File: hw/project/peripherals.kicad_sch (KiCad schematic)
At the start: 71 parts, among them J1 Battery, J10 2.54 Comm, J11 Voltage Monitor, J12 SPI, J13 I2C, J14 CONN HEADER VERT 10POS 2MM, J2 Hall, J3 FTSH-107-01-L-DV-K-A, J4 Serial, J5 Phases, J8 Throttle, J9 CAN, SW3 USER, U2 ATA6561-GAQW-N

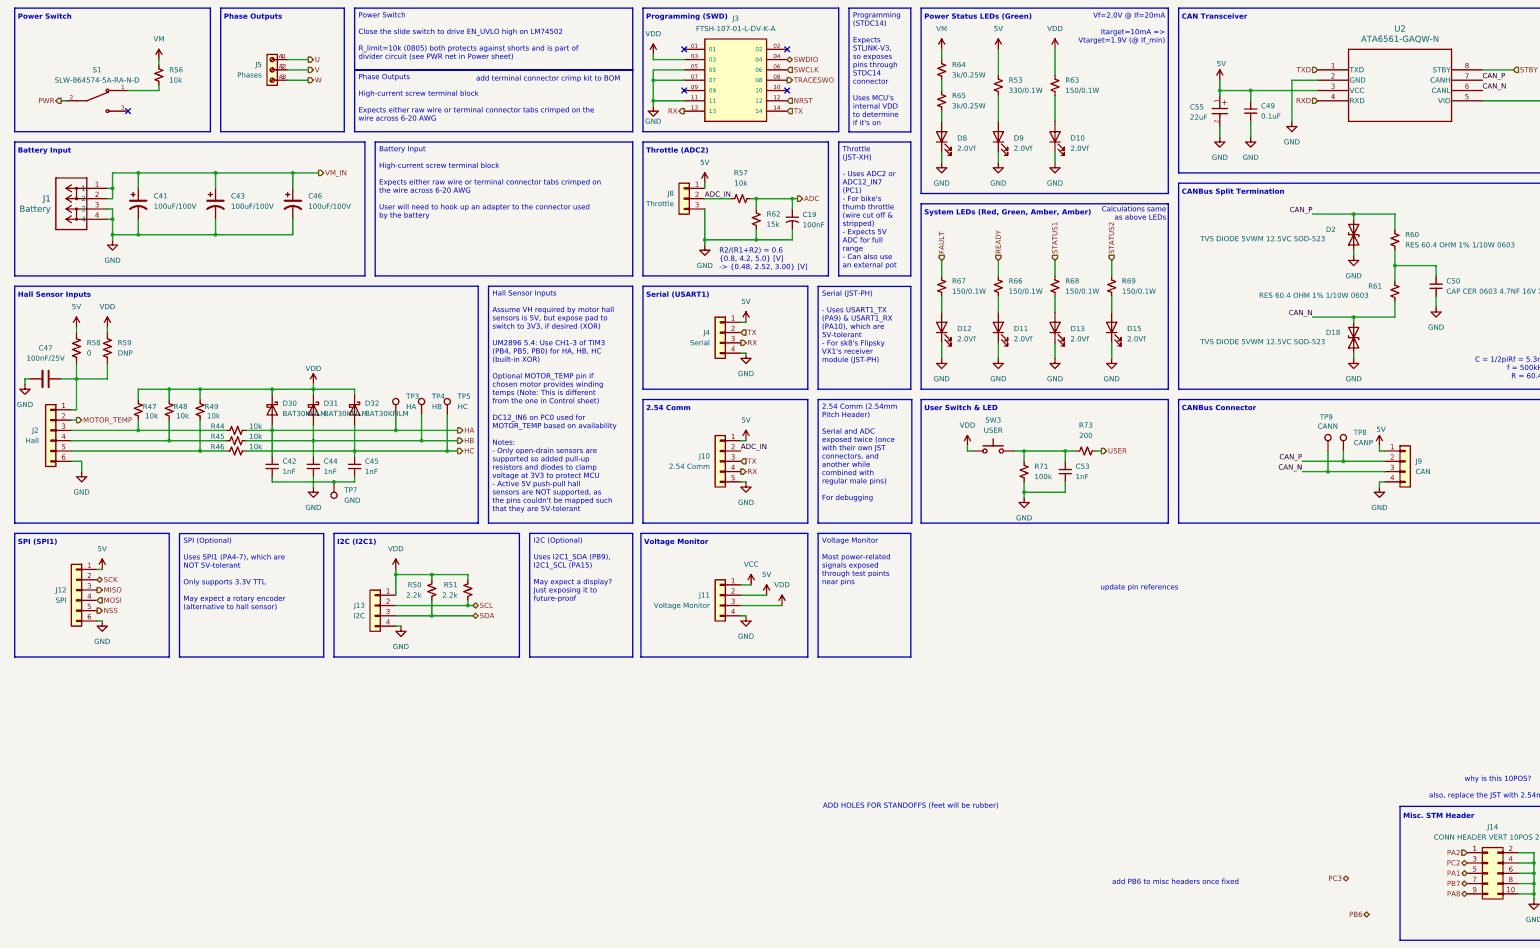
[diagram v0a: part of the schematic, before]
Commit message: Prettify root sheet
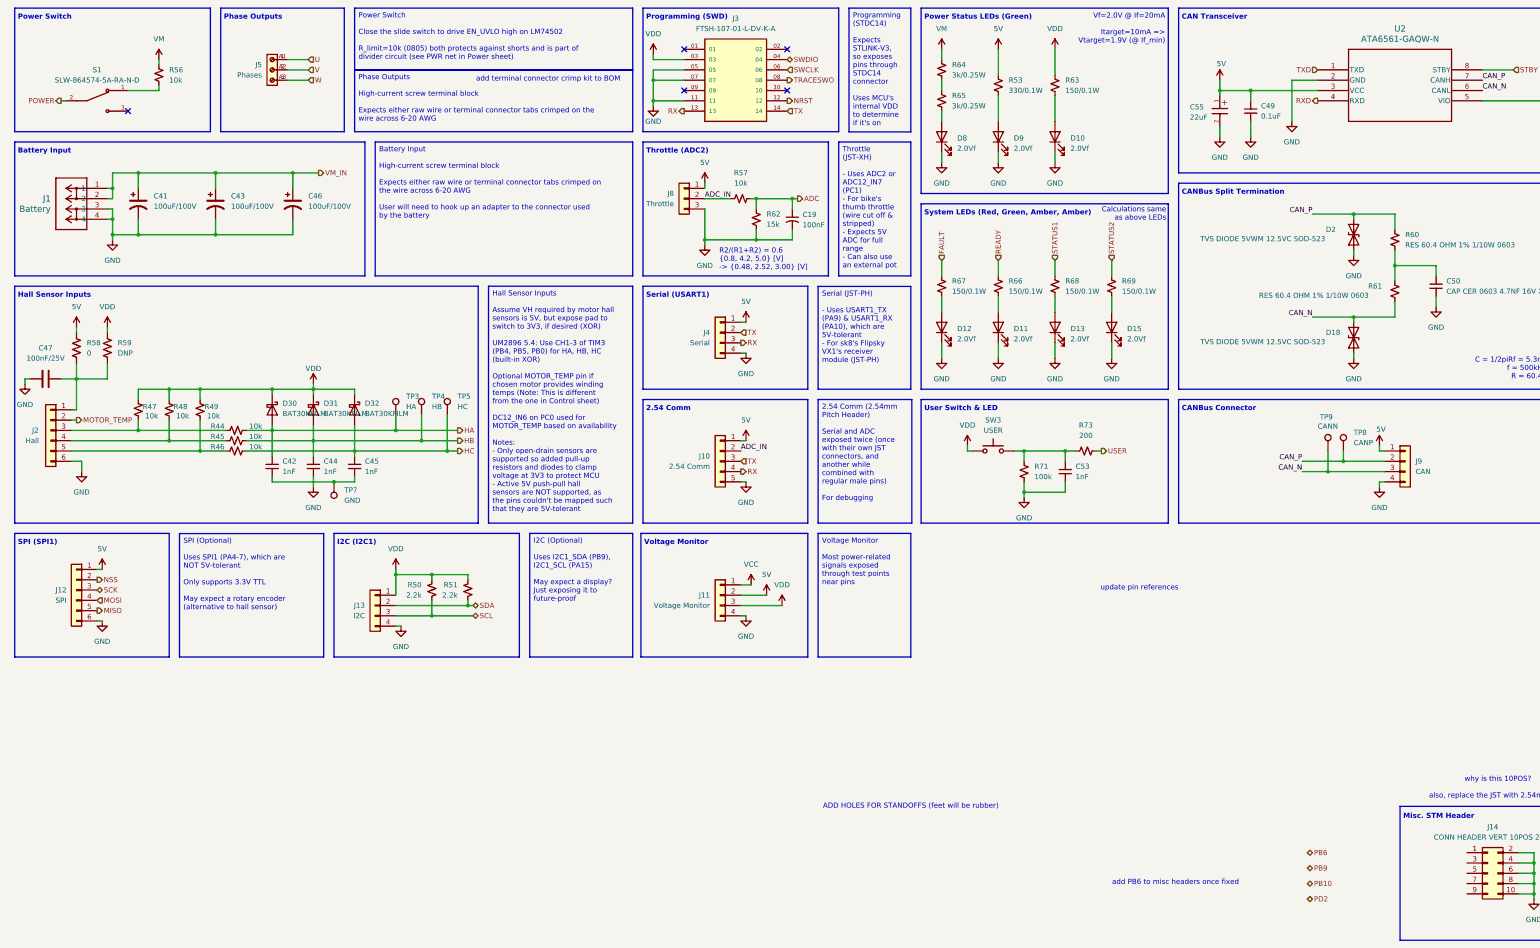
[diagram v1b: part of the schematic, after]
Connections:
- net MISO: now also J12.5 (Pin_5); no longer J12.3 (Pin_3)
- net NSS: now also J12.2 (Pin_2); no longer J12.5 (Pin_5)
- net SCK: now also J12.3 (Pin_3); no longer J12.2 (Pin_2)
- net SCL: now also J13.3 (Pin_3), R50.2; no longer J13.2 (Pin_2), R51.2
- net SDA: now also J13.2 (Pin_2), R51.2; no longer J13.3 (Pin_3), R50.2
- net PA1: no longer names the net of J14.5 (Pin_5)
- net PA2: no longer names the net of J14.1 (Pin_1)
- net PA8: no longer names the net of J14.9 (Pin_9)
- net PB7: no longer names the net of J14.7 (Pin_7)
- net PC2: no longer names the net of J14.3 (Pin_3)
- net PWR renamed POWER

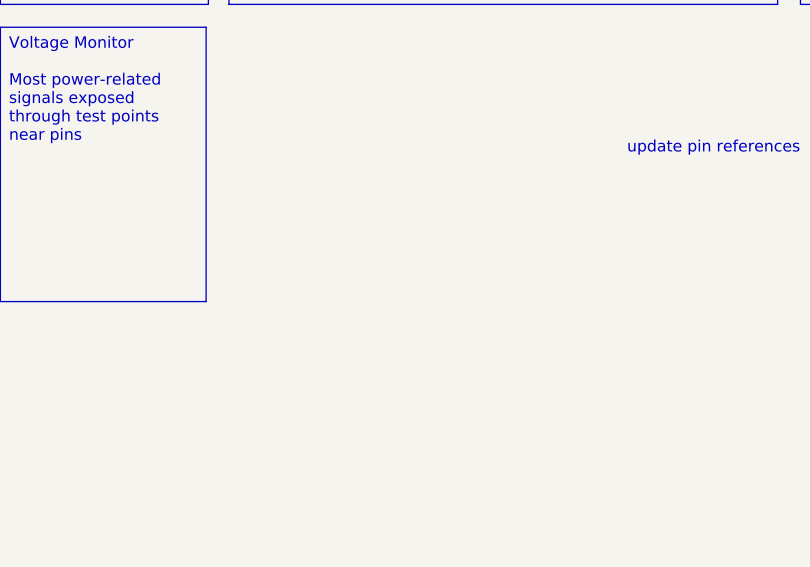
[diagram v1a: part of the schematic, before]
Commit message: Finished control sheet sensing. Need to work on OSC tomorrow
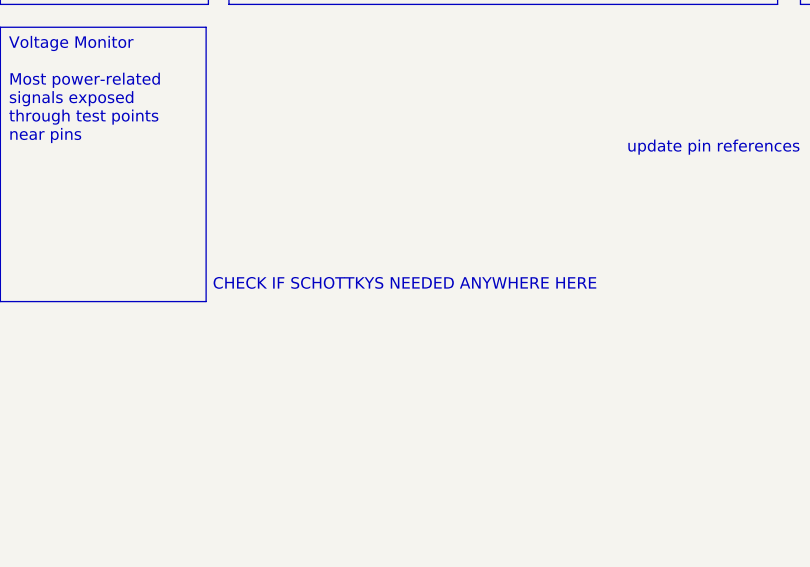
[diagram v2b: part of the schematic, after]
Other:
- note added: "CHECK IF SCHOTTKYS NEEDED ANYWHERE HERE"
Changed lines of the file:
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@@
+		)
+	)
+	(text "CHECK IF SCHOTTKYS NEEDED ANYWHERE HERE"
+		(exclude_from_sim no)
+		(at 258.318 176.022 0)
+		(effects
+			(font
+				(size 1.27 1.27)
+				(color 255 4 4 1)
+			)
 		)
 	)

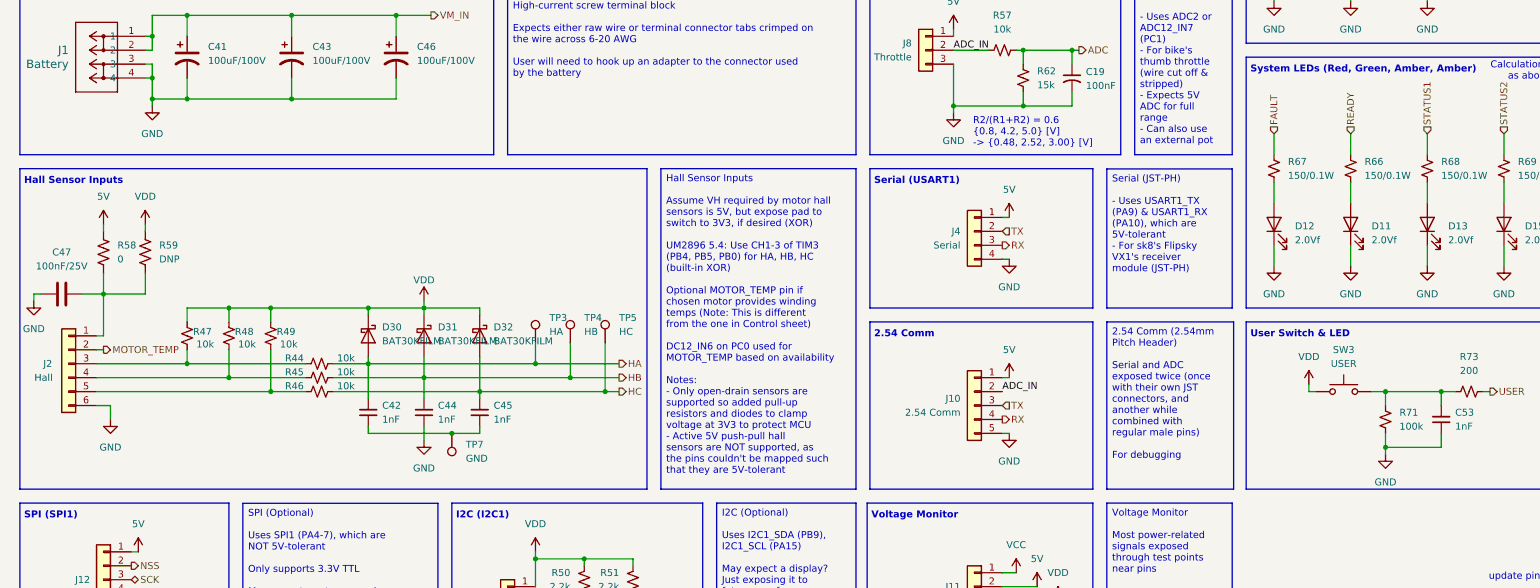
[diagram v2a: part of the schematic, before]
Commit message: Finalize phase voltage sensing
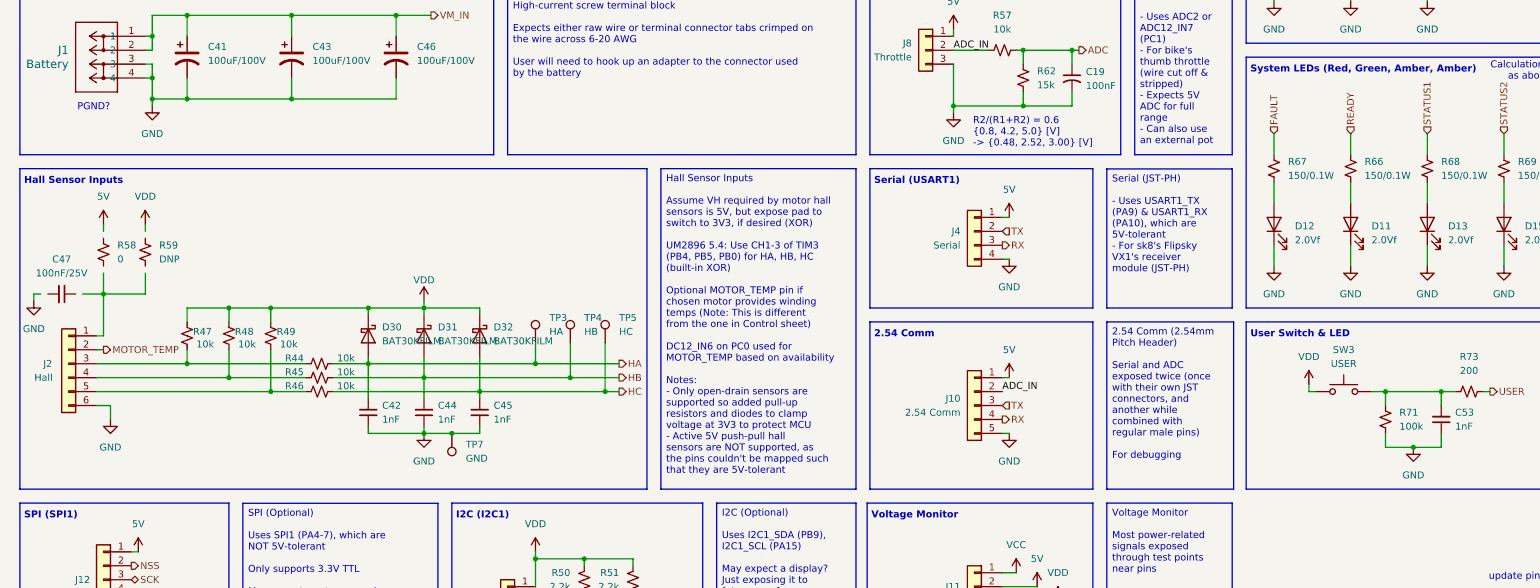
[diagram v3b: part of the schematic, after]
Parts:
- C47: symbol Device:C -> Device:C_Small
- R58, R59: symbol Device:R_US -> Device:R_Small_US
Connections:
- net 5V: no longer R58.1
- net GND: now also C42.1, C45.1, TP7.1; no longer C47.2
- net VDD: no longer R59.1
- now unconnected: C47.1, J2.1 (Pin_1), R58.2, R59.2
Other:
- note added: "PGND?"
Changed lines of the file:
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@@
 		)
 	)
+	(text "PGND?"
+		(exclude_from_sim no)
+		(at 28.702 75.184 0)
+		(effects
+			(font
+				(size 1.27 1.27)
+				(color 255 4 4 1)
+			)
+		)
+	)
 	(text "Power Switch"
 		(exclude_from_sim no)
@@
 	)
 	(junction
+		(at 269.24 137.16)
+		(diameter 0)
+		(color 0 0 0 0)
+	)
+	(junction
 		(at 172.72 35.56)
 		(diameter 0)
@@
 	)
 	(junction
-		(at 345.44 93.98)
+		(at 88.9 134.62)
 		(diameter 0)
 		(color 0 0 0 0)
 	)
 	(junction
-		(at 45.72 58.42)
+		(at 345.44 93.98)
 		(diameter 0)
 		(color 0 0 0 0)
 	)
 	(junction
-		(at 118.11 167.64)
+		(at 45.72 58.42)
 		(diameter 0)
 		(color 0 0 0 0)
 	)
 	(junction
-		(at 264.16 137.16)
+		(at 118.11 167.64)
 		(diameter 0)
 		(color 0 0 0 0)
@@
 	(wire
 		(pts
+			(xy 269.24 137.16) (xy 274.32 137.16)
+		)
+		(stroke
+			(width 0)
+			(type default)
+		)
+	)
+	(wire
+		(pts
 			(xy 60.96 111.76) (xy 60.96 114.3)
 		)
@@
 	(wire
 		(pts
+			(xy 88.9 134.62) (xy 93.98 134.62)
+		)
+		(stroke
+			(width 0)
+			(type default)
+		)
+	)
+	(wire
+		(pts
 			(xy 386.08 236.22) (xy 389.89 236.22)
 		)
@@
 	(wire
 		(pts
-			(xy 88.9 133.35) (xy 88.9 135.89)
+			(xy 88.9 133.35) (xy 88.9 134.62)
 		)
 		(stroke
@@
 	(wire
 		(pts
-			(xy 264.16 137.16) (xy 264.16 138.43)
-		)
-		(stroke
-			(width 0)
-			(type default)
-		)
-	)
-	(wire
-		(pts
 			(xy 250.19 127) (xy 251.46 127)
 		)
@@
 	(wire
 		(pts
-			(xy 264.16 137.16) (xy 274.32 137.16)
+			(xy 264.16 137.16) (xy 269.24 137.16)
 		)
 		(stroke
@@
 	(wire
 		(pts
-			(xy 78.74 134.62) (xy 93.98 134.62)
+			(xy 78.74 134.62) (xy 88.9 134.62)
 		)
 		(stroke
@@
 	)
 	(symbol
-		(lib_id "Device:R_US")
+		(lib_id "Device:R_Small_US")
 		(at 30.48 101.6 0)
 		(unit 1)
@@
 		)
 		(property "Footprint" "Resistor_SMD:R_0805_2012Metric_Pad1.20x1.40mm_HandSolder"
-			(at 31.496 101.854 90)
+			(at 30.48 101.6 0)
 			(hide yes)
 			(show_name no)
@@
 			)
 		)
-		(property "Description" "Resistor, US symbol"
+		(property "Description" "Resistor, small US symbol"
 			(at 30.48 101.6 0)
 			(hide yes)
@@
 	)
 	(symbol
-		(lib_id "Device:C")
+		(lib_id "Device:C_Small")
 		(at 22.86 109.22 270)
 		(unit 1)
@@
 		(fields_autoplaced yes)
 		(property "Reference" "C47"
-			(at 22.86 101.6 90)
+			(at 22.8536 102.87 90)
 			(show_name no)
 			(do_not_autoplace no)
@@
 		)
 		(property "Value" "100nF/25V"
-			(at 22.86 104.14 90)
+			(at 22.8536 105.41 90)
 			(show_name no)
 			(do_not_autoplace no)
@@
 		)
 		(property "Footprint" "Capacitor_SMD:C_0805_2012Metric_Pad1.18x1.45mm_HandSolder"
-			(at 19.05 110.1852 0)
+			(at 22.86 109.22 0)
 			(hide yes)
 			(show_name no)
@@
 			)
 		)
-		(property "Description" "Unpolarized capacitor"
+		(property "Description" "Unpolarized capacitor, small symbol"
 			(at 22.86 109.22 0)
 			(hide yes)
@@
 	)
 	(symbol
-		(lib_id "Device:R_US")
+		(lib_id "Device:R_Small_US")
 		(at 38.1 101.6 0)
 		(unit 1)
@@
 		)
 		(property "Footprint" "Resistor_SMD:R_0805_2012Metric_Pad1.20x1.40mm_HandSolder"
-			(at 39.116 101.854 90)
+			(at 38.1 101.6 0)
 			(hide yes)
 			(show_name no)
@@
 			)
 		)
-		(property "Description" "Resistor, US symbol"
+		(property "Description" "Resistor, small US symbol"
 			(at 38.1 101.6 0)
 			(hide yes)
@@
 	(symbol
 		(lib_id "power:GND")
-		(at 264.16 138.43 0)
+		(at 269.24 137.16 0)
 		(unit 1)
 		(body_style 1)
@@
 		(fields_autoplaced yes)
 		(property "Reference" "#PWR0122"
-			(at 264.16 144.78 0)
+			(at 269.24 143.51 0)
 			(hide yes)
 			(show_name no)
@@
 		)
 		(property "Value" "GND"
-			(at 264.16 143.51 0)
+			(at 269.24 142.24 0)
 			(show_name no)
 			(do_not_autoplace no)
@@
 		)
 		(property "Footprint" ""
-			(at 264.16 138.43 0)
+			(at 269.24 137.16 0)
 			(hide yes)
 			(show_name no)
@@
 		)
 		(property "Datasheet" ""
-			(at 264.16 138.43 0)
+			(at 269.24 137.16 0)
 			(hide yes)
 			(show_name no)
@@
 		)
 		(property "Description" "Power symbol creates a global label with name \"GND\" , ground"
-			(at 264.16 138.43 0)
+			(at 269.24 137.16 0)
 			(hide yes)
 			(show_name no)
@@
 	(symbol
 		(lib_id "power:GND")
-		(at 88.9 135.89 0)
+		(at 88.9 134.62 0)
 		(mirror y)
 		(unit 1)
@@
 		(fields_autoplaced yes)
 		(property "Reference" "#PWR080"
-			(at 88.9 142.24 0)
+			(at 88.9 140.97 0)
 			(hide yes)
 			(show_name no)
@@
 		)
 		(property "Value" "GND"
-			(at 88.9 140.97 0)
+			(at 88.9 139.7 0)
 			(show_name no)
 			(do_not_autoplace no)
@@
 		)
 		(property "Footprint" ""
-			(at 88.9 135.89 0)
+			(at 88.9 134.62 0)
 			(hide yes)
 			(show_name no)
@@
 		)
 		(property "Datasheet" ""
-			(at 88.9 135.89 0)
+			(at 88.9 134.62 0)
 			(hide yes)
 			(show_name no)
@@
 		)
 		(property "Description" "Power symbol creates a global label with name \"GND\" , ground"
-			(at 88.9 135.89 0)
+			(at 88.9 134.62 0)
 			(hide yes)
 			(show_name no)

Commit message: Finalize drive sheet
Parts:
- removed C42, C44, C45: 1nF, Capacitor_SMD:C_0603_1608Metric_Pad1.08x0.95mm_HandSolder, symbol Device:C_Small
- removed C53: 1nF, Capacitor_SMD:C_0603_1608Metric, symbol Device:C_Small
- added C60, C61, C62, C63: 1nF, Capacitor_SMD:C_0603_1608Metric, symbol Device:C_Small
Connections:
- net GND: now also C60.1, C61.1, C62.1, C63.1; no longer C41.2, C43.2, C46.2, J1.3, J1.4
- net HA: now also C60.2
- net HB: now also C61.2
- net HC: now also C62.2
- net at R71.2, R73.2, SW3.2: now also C63.2
- new net PGND: C41.2, C43.2, C46.2, J1.3, J1.4
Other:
- note removed: "PGND?"
